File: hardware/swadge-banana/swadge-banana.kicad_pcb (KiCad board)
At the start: 2 copper layers, 85 x 173.2 mm, 47 parts, among them J1 USB_B_Micro, SW1 SW_SPDT, U1 AP1117-33, U2 ESP-13-WROOM-02D, U3 BUS_PCIexpress, U4 OLED_CONNECTOR, U5 QMA6981, U6 OLED_DISPLAY

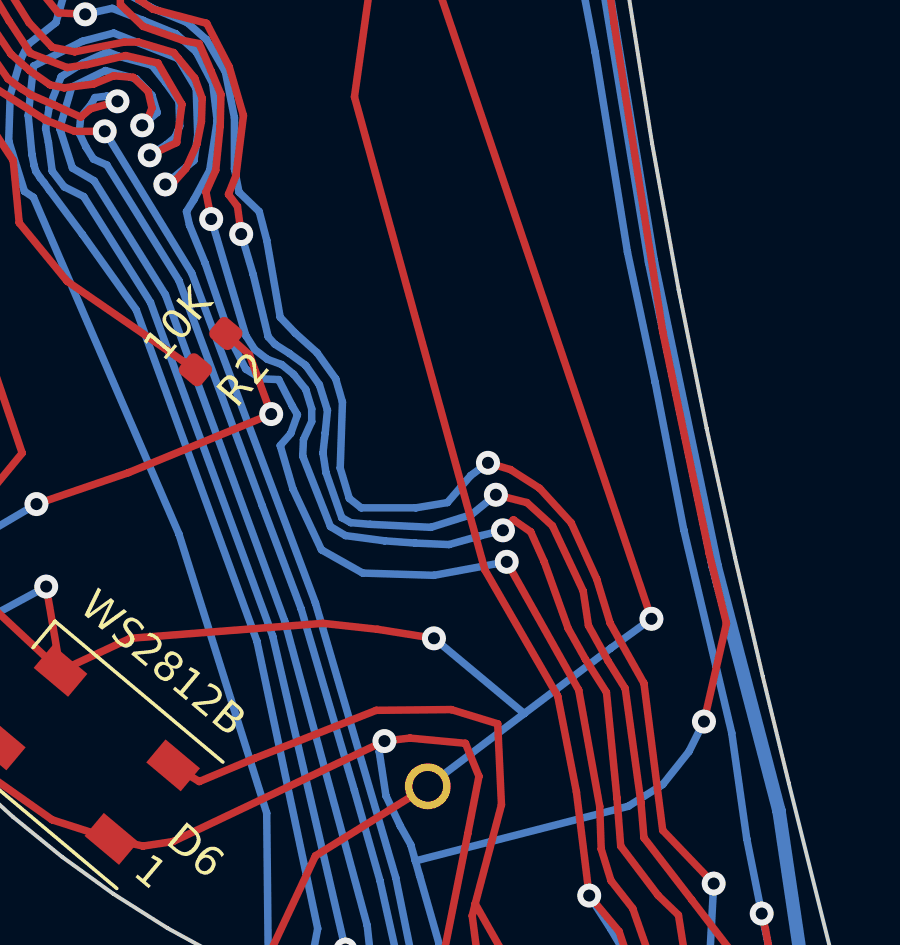
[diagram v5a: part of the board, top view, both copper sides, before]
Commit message: Added bananaraptor to swadge-banana
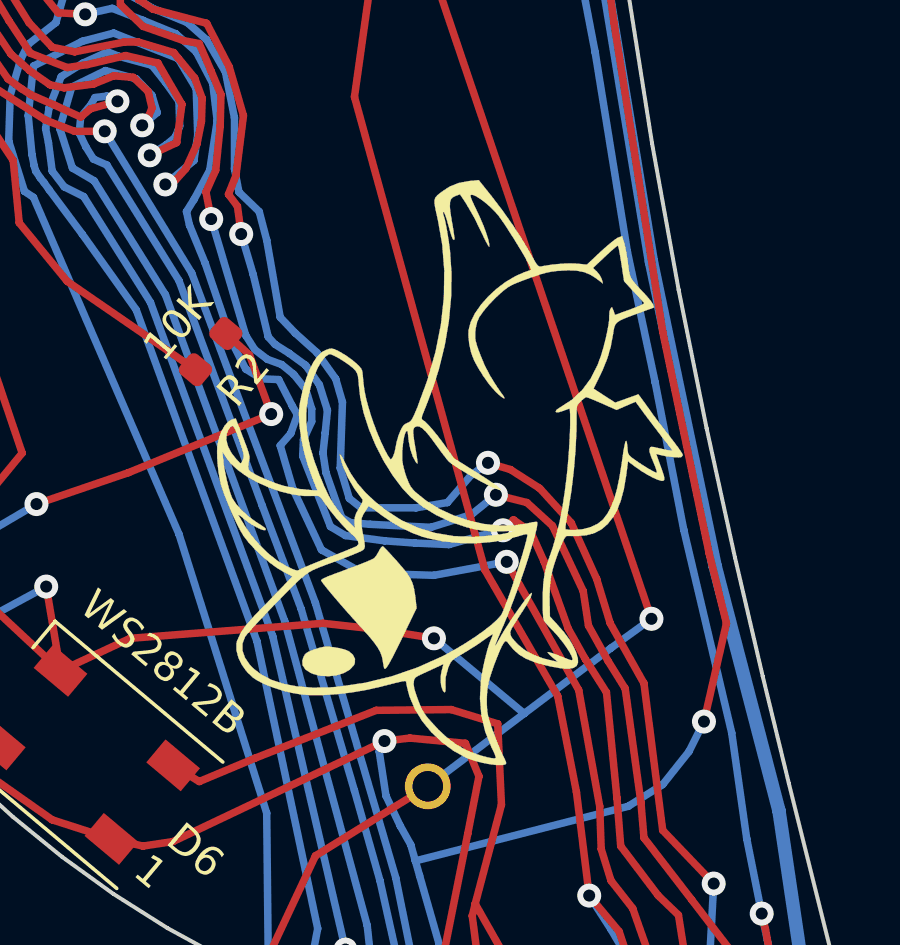
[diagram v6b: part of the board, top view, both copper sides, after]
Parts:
- added Ref**: Val**, Swadge_Parts:bananaraptor, F.Cu at (142.9, 165.4)

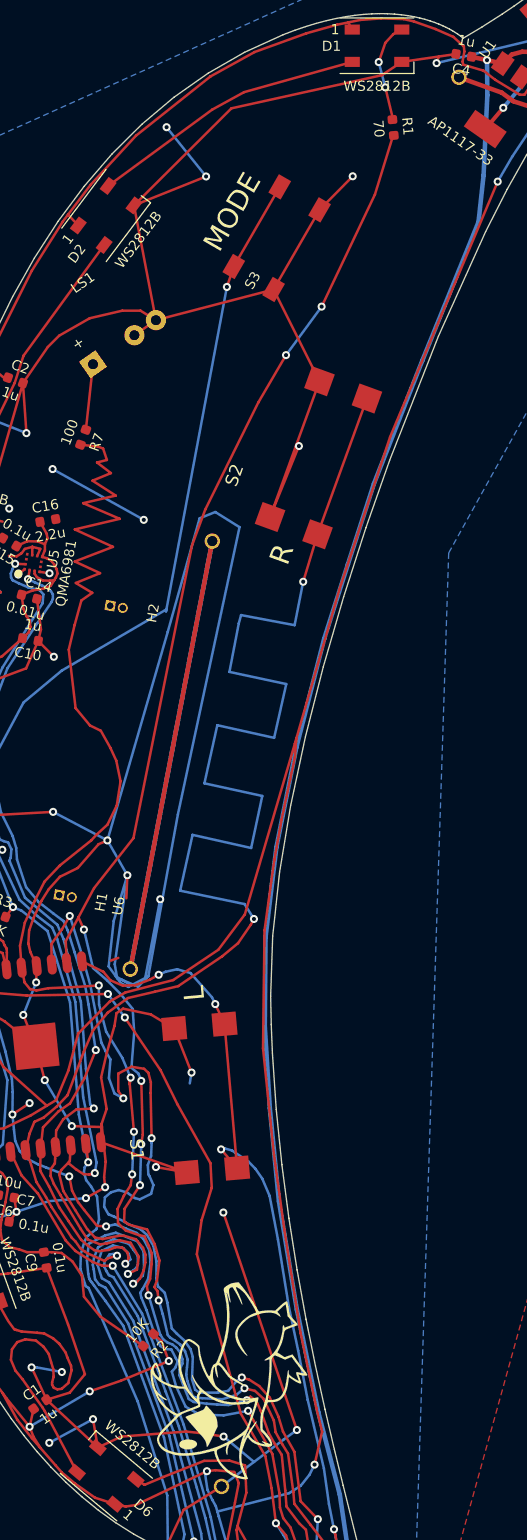
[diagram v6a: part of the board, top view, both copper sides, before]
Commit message: Added hole Moved R2, embiggened bananaraptor
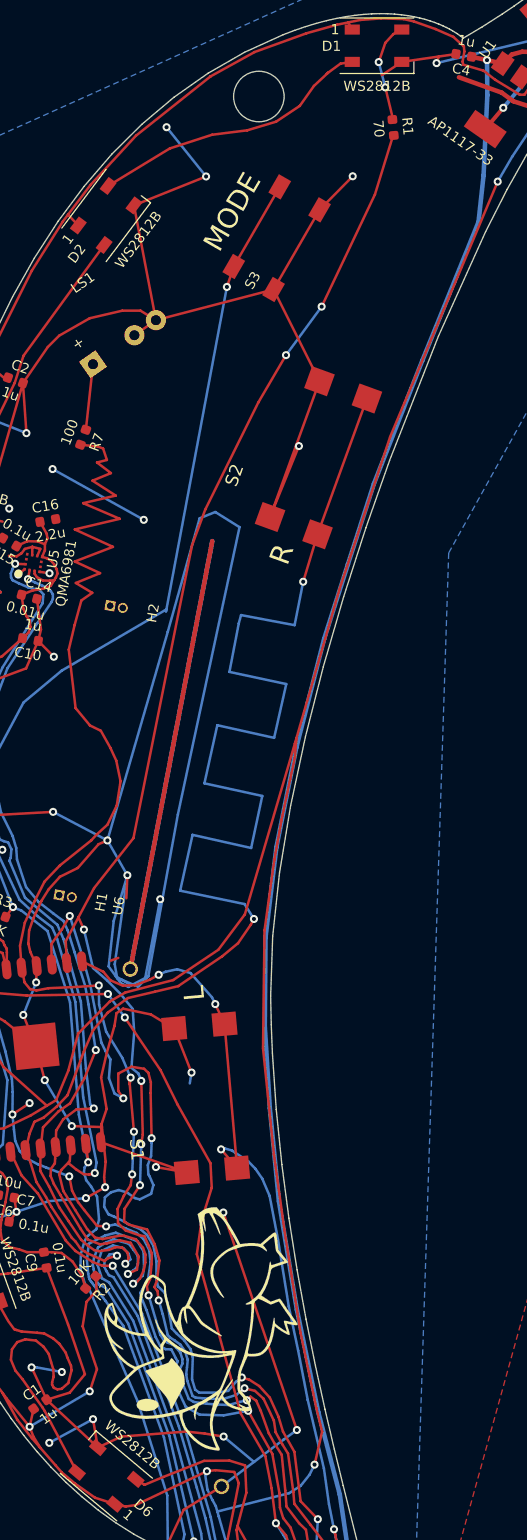
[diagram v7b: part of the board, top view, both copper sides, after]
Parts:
- removed BT2: Battery, Swadge_Parts:2460
- removed the Ref** at (142.9, 165.4)
- added Ref**: Val**, Swadge_Parts:bananaraptor_large, F.Cu at (140.1, 160.3)
- moved R2 8.07 mm to (129.3, 155.2)
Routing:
- net GND: track 698.4 -> 669.6 mm
- net Net-(C9-Pad2): track 28.3 -> 19.8 mm
- net +3V3: track 621.2 -> 621.8 mm, vias 10 -> 9
- net Net-(D1-Pad2): track 27.5 -> 28.0 mm
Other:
- outline, holes or cut-outs redrawn

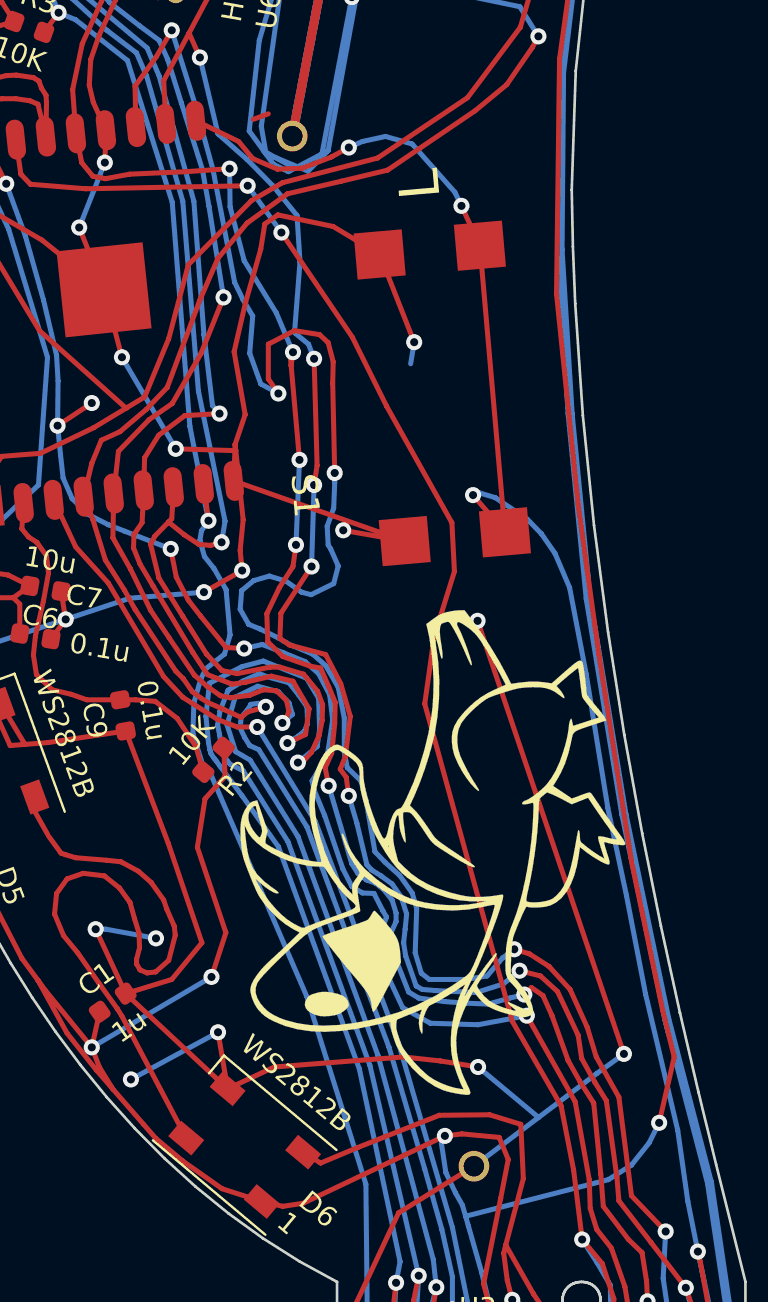
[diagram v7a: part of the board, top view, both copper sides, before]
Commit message: Moved R2 back to original position so stencil & pick-n-place won't change Made bananaraptor even bigger
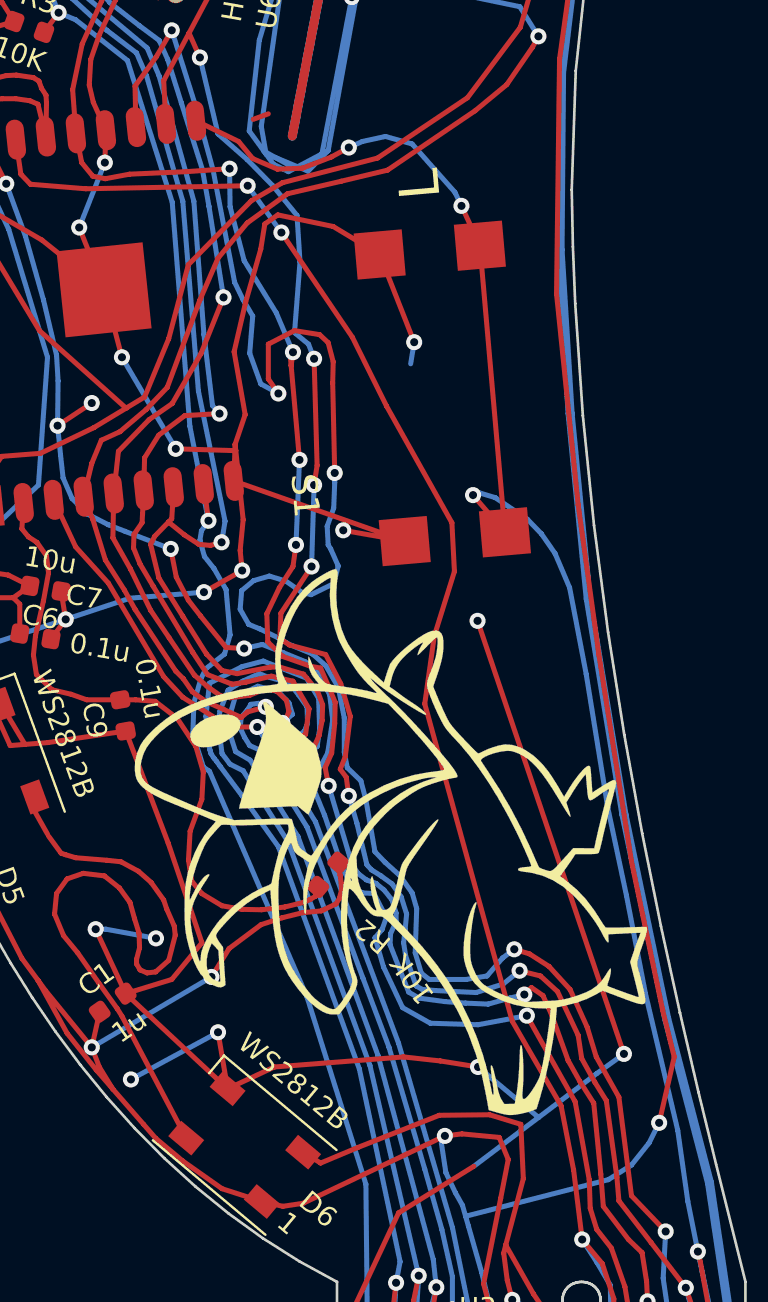
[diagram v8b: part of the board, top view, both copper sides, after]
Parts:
- removed BT1: Battery, Swadge_Parts:2460
- removed the Ref** at (140.1, 160.3)
- added Ref**: Val**, Swadge_Parts:bananaraptor_xl, F.Cu at (138.1, 159.4)
- moved R2 8.07 mm to (135.0, 160.9)
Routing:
- net Net-(C9-Pad2): track 19.8 -> 32.6 mm
- net +3V3: track 621.8 -> 619.3 mm
